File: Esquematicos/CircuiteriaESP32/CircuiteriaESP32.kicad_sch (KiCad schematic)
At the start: 14 parts, among them J1 Conn_01x19, J2 Conn_01x19

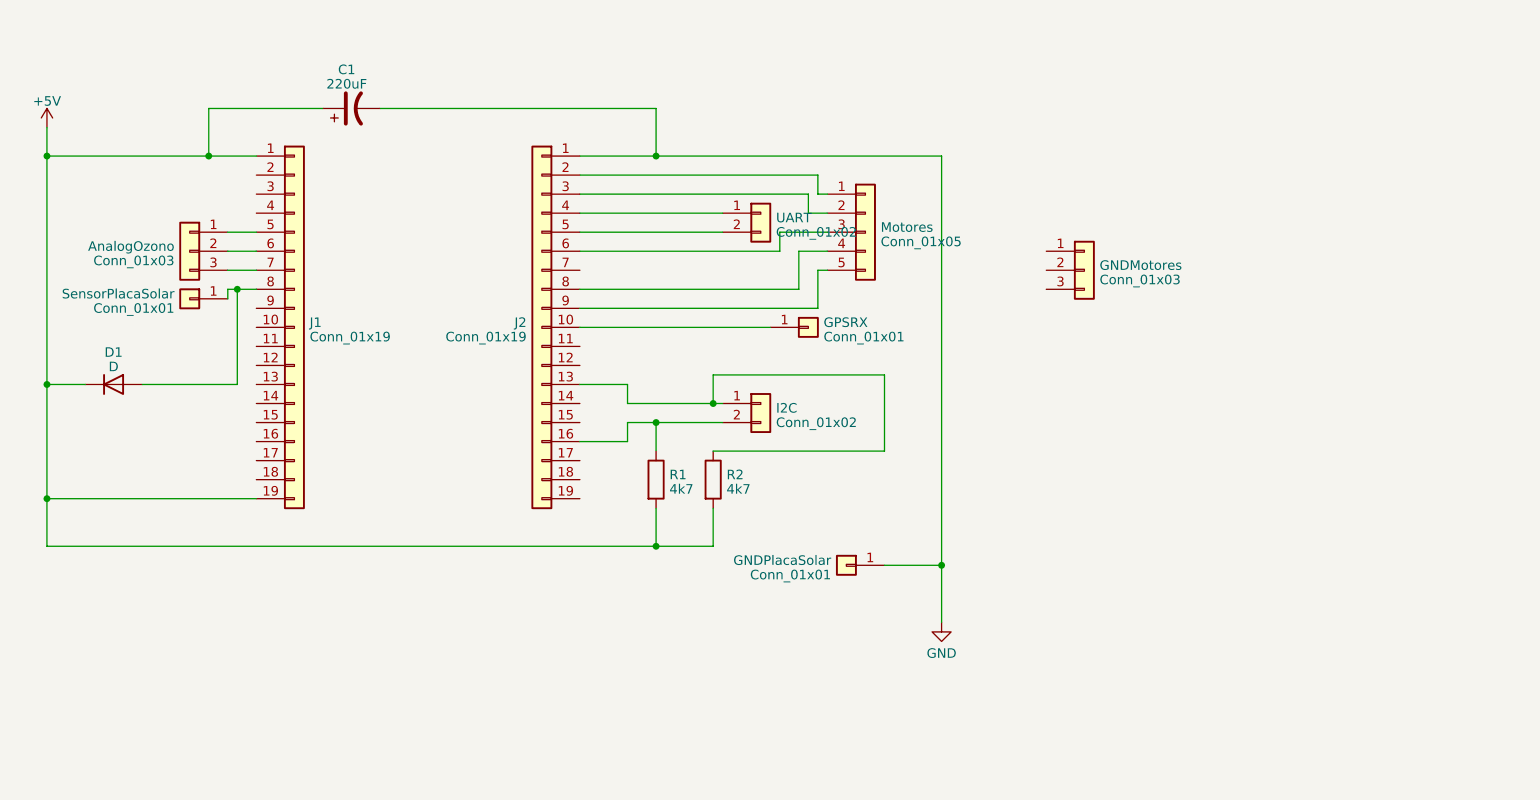
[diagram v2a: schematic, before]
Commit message: Añadido codigo para adafruit i2c
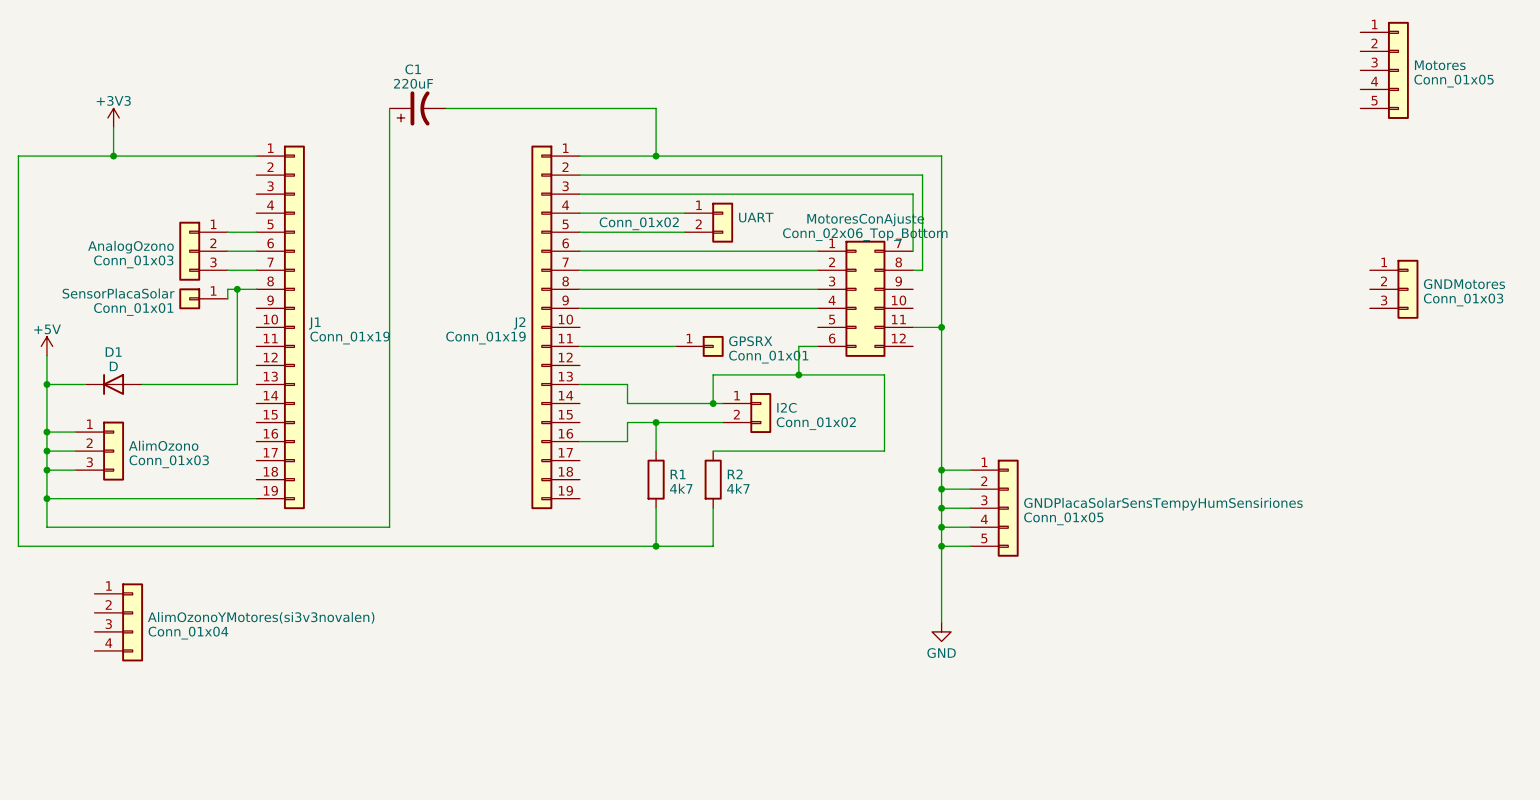
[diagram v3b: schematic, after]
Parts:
- removed GNDPlacaSolar: Conn_01x01, symbol Connector_Generic:Conn_01x01
- added AlimOzono: Conn_01x03, symbol Connector_Generic:Conn_01x03
- added AlimOzonoYMotores(si3v3novalen): Conn_01x04, symbol Connector_Generic:Conn_01x04
- added GNDPlacaSolarSensTempyHumSensiriones: Conn_01x05, symbol Connector_Generic:Conn_01x05
- added MotoresConAjuste: Conn_02x06_Top_Bottom, symbol Connector_Generic:Conn_02x06_Top_Bottom
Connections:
- net +5V: now also AlimOzono.1 (Pin_1), AlimOzono.2 (Pin_2), AlimOzono.3 (Pin_3); no longer J1.1 (Pin_1), R1.2, R2.2
- net GND: now also GNDPlacaSolarSensTempyHumSensiriones.1 (Pin_1), GNDPlacaSolarSensTempyHumSensiriones.2 (Pin_2), GNDPlacaSolarSensTempyHumSensiriones.3 (Pin_3), GNDPlacaSolarSensTempyHumSensiriones.4 (Pin_4), GNDPlacaSolarSensTempyHumSensiriones.5 (Pin_5), MotoresConAjuste.11 (Pin_11)
- net at GPSRX.1 (Pin_1): now also J2.11 (Pin_11); no longer J2.10 (Pin_10)
- net at I2C.1 (Pin_1), J2.13 (Pin_13), R2.1: now also MotoresConAjuste.6 (Pin_6)
- net at J2.2 (Pin_2): now also MotoresConAjuste.8 (Pin_8); no longer Motores.1 (Pin_1)
- net at J2.3 (Pin_3): now also MotoresConAjuste.7 (Pin_7); no longer Motores.2 (Pin_2)
- net at J2.6 (Pin_6): now also MotoresConAjuste.1 (Pin_1); no longer Motores.3 (Pin_3)
- net at J2.8 (Pin_8): now also MotoresConAjuste.3 (Pin_3); no longer Motores.4 (Pin_4)
- net at J2.9 (Pin_9): now also MotoresConAjuste.4 (Pin_4); no longer Motores.5 (Pin_5)
- net at J2.7 (Pin_7): now also MotoresConAjuste.2 (Pin_2)
- new net +3V3: J1.1 (Pin_1), R1.2, R2.2
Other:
- moved on the sheet: C1, GNDMotores, GPSRX, Motores, UART

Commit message: Esquematico actualizado
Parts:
- added I2CADCExterno: Conn_01x10, symbol Connector_Generic:Conn_01x10
- renumbered GPSRX to GPSTX
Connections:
- net +5V: now also I2CADCExterno.1 (Pin_1)
- net GND: now also I2CADCExterno.2 (Pin_2), I2CADCExterno.6 (Pin_6)
- net at AnalogOzono.1 (Pin_1): now also I2CADCExterno.7 (Pin_7); no longer J1.5 (Pin_5)
- net at AnalogOzono.2 (Pin_2): now also I2CADCExterno.8 (Pin_8); no longer J1.6 (Pin_6)
- net at AnalogOzono.3 (Pin_3): now also I2CADCExterno.9 (Pin_9); no longer J1.7 (Pin_7)
- net at GPSTX.1 (Pin_1): now also J2.10 (Pin_10); no longer J2.11 (Pin_11)
- net at I2C.1 (Pin_1), J2.13 (Pin_13), MotoresConAjuste.6 (Pin_6)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: now also I2CADCExterno.3 (Pin_3)
- net at I2C.2 (Pin_2), J2.16 (Pin_16), R1.1: now also I2CADCExterno.4 (Pin_4)
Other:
- moved on the sheet: AlimOzonoYMotores(si3v3novalen), AnalogOzono, GPSTX

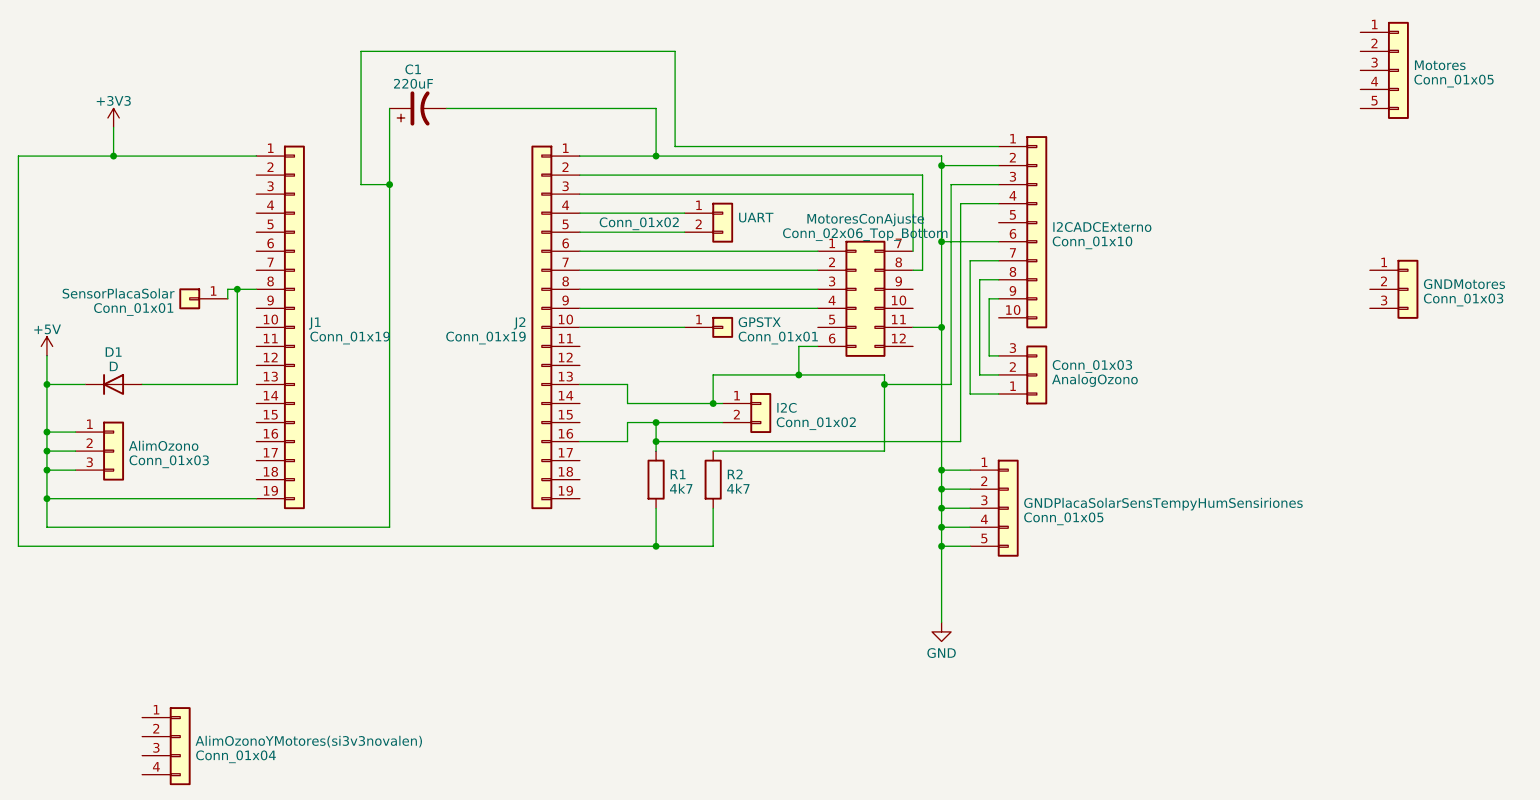
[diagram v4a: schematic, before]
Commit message: Arreglos para servos y algo de sensores
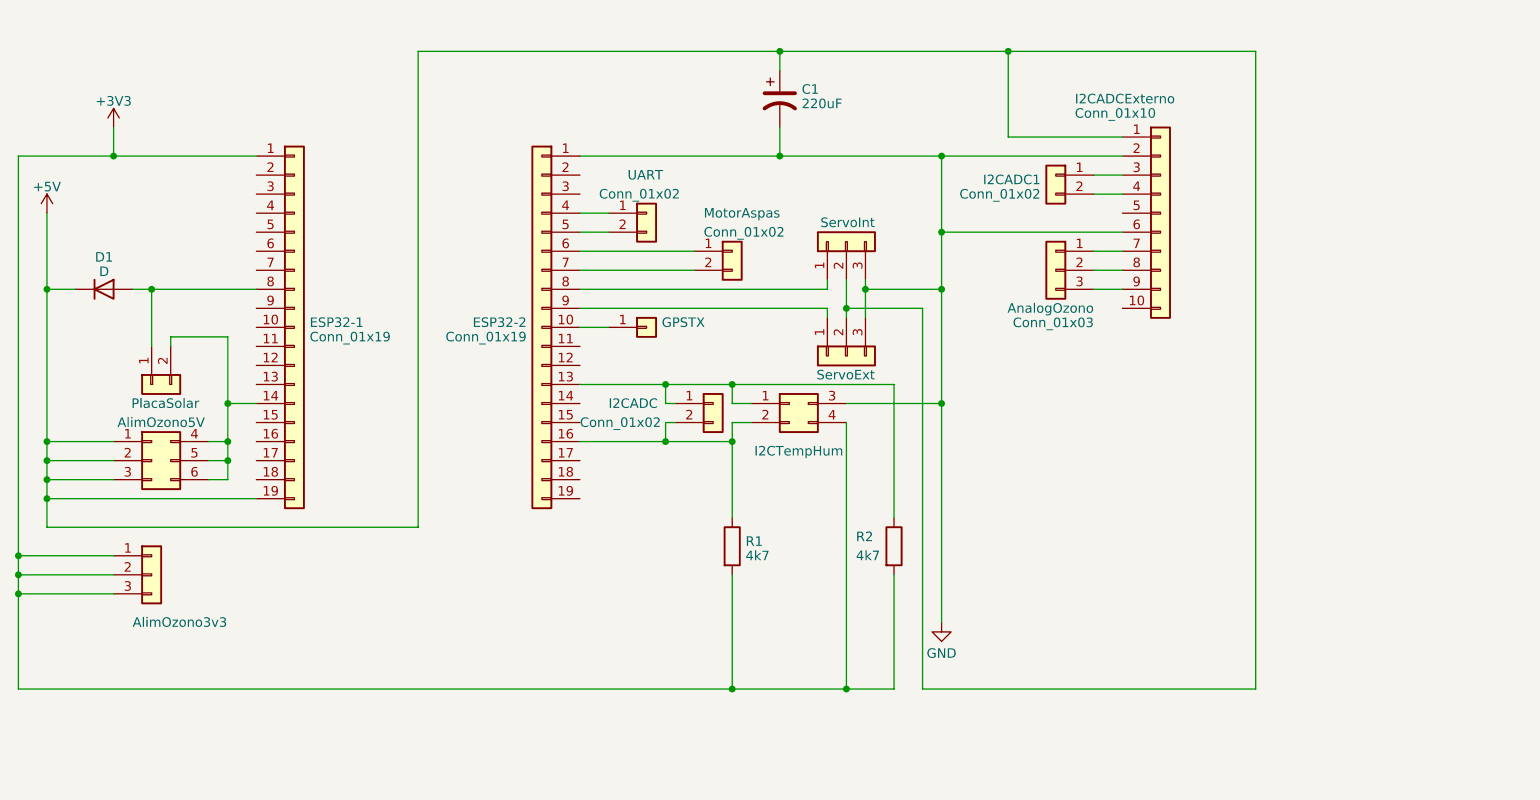
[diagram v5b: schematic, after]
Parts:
- removed AlimOzono, GNDMotores: Conn_01x03, symbol Connector_Generic:Conn_01x03
- removed AlimOzonoYMotores(si3v3novalen): Conn_01x04, symbol Connector_Generic:Conn_01x04
- removed GNDPlacaSolarSensTempyHumSensiriones, Motores: Conn_01x05, symbol Connector_Generic:Conn_01x05
- removed I2C: Conn_01x02, symbol Connector_Generic:Conn_01x02
- removed MotoresConAjuste: Conn_02x06_Top_Bottom, symbol Connector_Generic:Conn_02x06_Top_Bottom
- removed SensorPlacaSolar: Conn_01x01, symbol Connector_Generic:Conn_01x01
- added AlimOzono3v3, ServoExt, ServoInt: Conn_01x03, symbol Connector_Generic:Conn_01x03
- added AlimOzono5V: Conn_02x03_Top_Bottom, symbol Connector_Generic:Conn_02x03_Top_Bottom
- added I2CADC, I2CADC1, MotorAspas, PlacaSolar: Conn_01x02, symbol Connector_Generic:Conn_01x02
- added I2CTempHum: Conn_02x02_Top_Bottom, symbol Connector_Generic:Conn_02x02_Top_Bottom
- renumbered J1 to ESP32-1, J2 to ESP32-2
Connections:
- net +3V3: now also AlimOzono3v3.1 (Pin_1), AlimOzono3v3.2 (Pin_2), AlimOzono3v3.3 (Pin_3), I2CTempHum.4 (Pin_4)
- net +5V: now also AlimOzono5V.1 (Pin_1), AlimOzono5V.2 (Pin_2), AlimOzono5V.3 (Pin_3), ServoExt.2 (Pin_2), ServoInt.2 (Pin_2)
- net GND: now also I2CTempHum.3 (Pin_3), ServoExt.3 (Pin_3), ServoInt.3 (Pin_3)
- net at ESP32-2.6 (Pin_6): now also MotorAspas.1 (Pin_1)
- net at ESP32-2.7 (Pin_7): now also MotorAspas.2 (Pin_2)
- net at ESP32-2.8 (Pin_8): now also ServoInt.1 (Pin_1)
- net at ESP32-2.9 (Pin_9): now also ServoExt.1 (Pin_1)
- net at ESP32-2.13 (Pin_13), R2.1: now also I2CADC.1 (Pin_1), I2CTempHum.1 (Pin_1); no longer I2CADCExterno.3 (Pin_3)
- net at D1.2 (A), ESP32-1.8 (Pin_8): now also PlacaSolar.1 (Pin_1)
- net at ESP32-2.16 (Pin_16), R1.1: now also I2CADC.2 (Pin_2), I2CTempHum.2 (Pin_2); no longer I2CADCExterno.4 (Pin_4)
- net at ESP32-1.14 (Pin_14): now also AlimOzono5V.4 (Pin_4), AlimOzono5V.5 (Pin_5), AlimOzono5V.6 (Pin_6), PlacaSolar.2 (Pin_2)
- new net: I2CADC1.1 (Pin_1), I2CADCExterno.3 (Pin_3)
- new net: I2CADC1.2 (Pin_2), I2CADCExterno.4 (Pin_4)
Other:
- moved on the sheet: AnalogOzono, C1, D1, GPSTX, I2CADCExterno, R1, R2, UART

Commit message: Actualización motores
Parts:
- removed MotorAspas: Conn_01x02, symbol Connector_Generic:Conn_01x02
- added AlimGPS: Conn_01x02, symbol Connector_Generic:Conn_01x02
- added MotorAspas, PuenteHAspas: Conn_01x04, symbol Connector_Generic:Conn_01x04
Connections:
- net +3V3: now also AlimGPS.1 (Pin_1)
- net +5V: now also PuenteHAspas.4 (Pin_4)
- net GND: now also PuenteHAspas.2 (Pin_2), PuenteHAspas.3 (Pin_3)
- net at ESP32-2.6 (Pin_6): now also PuenteHAspas.1 (Pin_1)
- net at ESP32-2.7 (Pin_7): now also AlimGPS.2 (Pin_2)

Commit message: Arreglos
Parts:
- removed MotorAspas: Conn_01x04, symbol Connector_Generic:Conn_01x04
- added D2: D, symbol Device:D
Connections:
- net +5V: now also D2.1 (K)
- net at D1.2 (A), ESP32-1.8 (Pin_8), PlacaSolar.1 (Pin_1): now also D2.2 (A)
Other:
- moved on the sheet: UART

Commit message: 23 Marzo 2023
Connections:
- net GND: now also I2CADCExterno.5 (Pin_5); no longer I2CADCExterno.6 (Pin_6)
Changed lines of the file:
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@@
   (junction (at 162.56 31.75) (diameter 0) (color 0 0 0 0)
   )
+  (junction (at 184.15 53.34) (diameter 0) (color 0 0 0 0)
+  )
   (junction (at 73.66 45.72) (diameter 0) (color 0 0 0 0)
   )
@@
   (junction (at 60.96 104.14) (diameter 0) (color 0 0 0 0)
   )
-  (junction (at 184.15 55.88) (diameter 0) (color 0 0 0 0)
-  )
   (junction (at 156.21 83.82) (diameter 0) (color 0 0 0 0)
   )
@@
     (stroke (width 0) (type default))
   )
+  (wire (pts (xy 184.15 53.34) (xy 184.15 78.74))
+    (stroke (width 0) (type default))
+  )
   (wire (pts (xy 120.65 95.25) (xy 120.65 116.84))
     (stroke (width 0) (type default))
@@
     (stroke (width 0) (type default))
   )
-  (wire (pts (xy 184.15 55.88) (xy 208.28 55.88))
-    (stroke (width 0) (type default))
-  )
   (wire (pts (xy 110.49 31.75) (xy 162.56 31.75))
     (stroke (width 0) (type default))
@@
     (stroke (width 0) (type default))
   )
-  (wire (pts (xy 110.49 31.75) (xy 110.49 95.25))
+  (wire (pts (xy 110.49 31.75) (xy 110.49 93.98))
     (stroke (width 0) (type default))
   )
@@
     (stroke (width 0) (type default))
   )
-  (wire (pts (xy 64.77 95.25) (xy 110.49 95.25))
+  (wire (pts (xy 64.77 93.98) (xy 110.49 93.98))
     (stroke (width 0) (type default))
   )
@@
     (stroke (width 0) (type default))
   )
-  (wire (pts (xy 111.76 59.69) (xy 111.76 96.52))
-    (stroke (width 0) (type default))
-  )
-  (wire (pts (xy 64.77 91.44) (xy 64.77 95.25))
+  (wire (pts (xy 116.84 59.69) (xy 116.84 96.52))
+    (stroke (width 0) (type default))
+  )
+  (wire (pts (xy 64.77 91.44) (xy 64.77 93.98))
     (stroke (width 0) (type default))
   )
@@
     (stroke (width 0) (type default))
   )
-  (wire (pts (xy 62.23 96.52) (xy 111.76 96.52))
-    (stroke (width 0) (type default))
-  )
-  (wire (pts (xy 111.76 59.69) (xy 163.83 59.69))
+  (wire (pts (xy 62.23 96.52) (xy 116.84 96.52))
+    (stroke (width 0) (type default))
+  )
+  (wire (pts (xy 116.84 59.69) (xy 163.83 59.69))
     (stroke (width 0) (type default))
   )
@@
     (stroke (width 0) (type default))
   )
-  (wire (pts (xy 184.15 45.72) (xy 184.15 55.88))
-    (stroke (width 0) (type default))
-  )
   (wire (pts (xy 156.21 78.74) (xy 156.21 76.2))
     (stroke (width 0) (type default))
@@
     (stroke (width 0) (type default))
   )
-  (wire (pts (xy 184.15 55.88) (xy 184.15 78.74))
+  (wire (pts (xy 184.15 45.72) (xy 184.15 53.34))
     (stroke (width 0) (type default))
   )
@@
     (stroke (width 0) (type default))
   )
+  (wire (pts (xy 184.15 53.34) (xy 208.28 53.34))
+    (stroke (width 0) (type default))
+  )
